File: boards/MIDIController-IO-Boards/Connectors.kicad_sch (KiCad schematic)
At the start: 26 parts, among them J1 KeyboardCtrl, J2 TechnicsCtrl, J3 StopLeftCtrl, J4 StopRightCtrl, J6 PanelCtrl, J7 ToeStudCtrl, U2 H11L1, U3 H11L1, U4 MAX3232

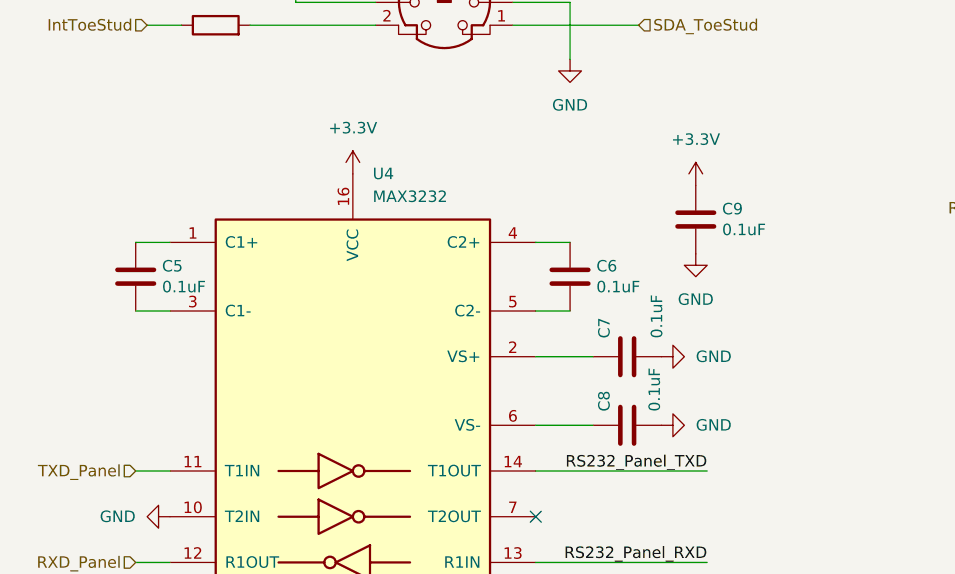
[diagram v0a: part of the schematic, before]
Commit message: Added bypass caps to power supplies, use cheaper MAX232 IC.
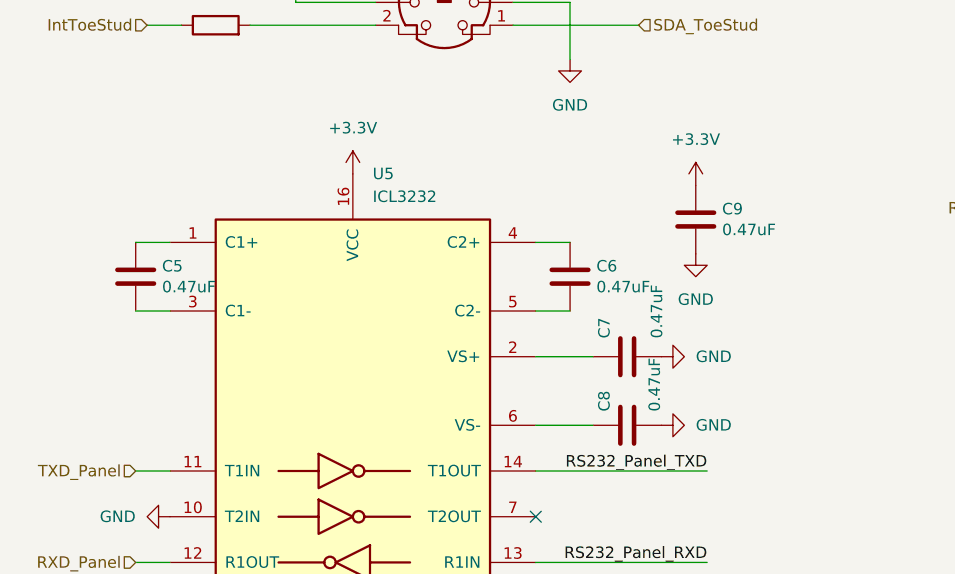
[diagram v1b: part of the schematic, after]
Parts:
- removed U4: MAX3232, Package_DIP:DIP-16_W7.62mm_Socket, symbol Interface_UART:MAX3232
- added U5: ICL3232, Package_DIP:DIP-16_W7.62mm, symbol Interface_UART:ICL3232
- C5, C6, C7, C8, C9: value 0.1uF -> 0.47uF
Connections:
- net +3.3V: now also U5.16 (VCC)
- net GND: now also U5.10 (T2IN), U5.15 (GND), U5.8 (R2IN)
- net RS232_Panel_RXD: now also U5.13 (R1IN)
- net RS232_Panel_TXD: now also U5.14 (T1OUT)
- net RXD_Panel: now also U5.12 (R1OUT)
- net TXD_Panel: now also U5.11 (T1IN)
- net at C6.1: now also U5.4 (C2+)
- net at C6.2: now also U5.5 (C2-)
- net at C5.1: now also U5.1 (C1+)
- net at C5.2: now also U5.3 (C1-)
- net at C7.1: now also U5.2 (VS+)
- net at C8.1: now also U5.6 (VS-)
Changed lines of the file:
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@@
+	)
+	(symbol
+		(lib_id "Interface_UART:ICL3232")
+		(at 142.24 125.73 0)
+		(unit 1)
+		(exclude_from_sim no)
+		(in_bom yes)
+		(on_board yes)
+		(dnp no)
+		(fields_autoplaced yes)
+		(property "Reference" "U5"
+			(at 144.4341 95.25 0)
+			(effects
+				(font
+					(size 1.27 1.27)
+				)
+				(justify left)
+			)
+		)
+		(property "Value" "ICL3232"
+			(at 144.4341 97.79 0)
+			(effects
+				(font
+					(size 1.27 1.27)
+				)
+				(justify left)
+			)
+		)
+		(property "Footprint" "Package_DIP:DIP-16_W7.62mm"
+			(at 143.51 152.4 0)
+			(effects
+				(font
+					(size 1.27 1.27)
+				)
+				(justify left)
+				(hide yes)
+			)
+		)
+		(property "Datasheet" "http://www.intersil.com/content/dam/Intersil/documents/icl3/icl3221-22-23-32-41-43.pdf"
+			(at 142.24 123.19 0)
+			(effects
+				(font
+					(size 1.27 1.27)
+				)
+				(hide yes)
+			)
+		)
+		(property "Description" "3.0V to 5.5V, Low-Power, up to 250kbps, True RS-232 Transceivers Using Four 0.1μF External Capacitors"
+			(at 142.24 125.73 0)
+			(effects
+				(font
+					(size 1.27 1.27)
+				)
+				(hide yes)
+			)
+		)
+		(pin "3"
+		)
+		(pin "8"
+		)
+		(pin "4"
+		)
+		(pin "2"
+		)
+		(pin "6"
+		)
+		(pin "7"
+		)
+		(pin "9"
+		)
+		(pin "5"
+		)
+		(pin "16"
+		)
+		(pin "14"
+		)
+		(pin "1"
+		)
+		(pin "15"
+		)
+		(pin "11"
+		)
+		(pin "12"
+		)
+		(pin "10"
+		)
+		(pin "13"
+		)
+		(instances
+			(project "MIDIController-IO-Boards"
+				(path "/06df47e9-b50a-4827-8ccb-76595e56d621/563c44a9-e62f-4884-9575-68843445bbb7"
+					(reference "U5")
+					(unit 1)
+				)
+			)
+		)
 	)
 	(symbol
@@
 			)
 		)
-		(property "Value" "0.1uF"
+		(property "Value" "0.47uF"
 			(at 183.261 101.473 0)
 			(effects
@@
 			)
 		)
-		(property "Value" "0.1uF"
+		(property "Value" "0.47uF"
 			(at 169.291 107.823 0)
 			(effects
@@
 			)
 		)
-		(property "Value" "0.1uF"
+		(property "Value" "0.47uF"
 			(at 121.031 107.823 0)
 			(effects
@@
 	)
 	(symbol
-		(lib_id "Interface_UART:MAX3232")
-		(at 142.24 125.73 0)
-		(unit 1)
-		(exclude_from_sim no)
-		(in_bom yes)
-		(on_board yes)
-		(dnp no)
-		(fields_autoplaced yes)
-		(property "Reference" "U4"
-			(at 144.4341 95.25 0)
-			(effects
-				(font
-					(size 1.27 1.27)
-				)
-				(justify left)
-			)
-		)
-		(property "Value" "MAX3232"
-			(at 144.4341 97.79 0)
-			(effects
-				(font
-					(size 1.27 1.27)
-				)
-				(justify left)
-			)
-		)
-		(property "Footprint" "Package_DIP:DIP-16_W7.62mm_Socket"
-			(at 143.51 152.4 0)
-			(effects
-				(font
-					(size 1.27 1.27)
-				)
-				(justify left)
-				(hide yes)
-			)
-		)
-		(property "Datasheet" "https://datasheets.maximintegrated.com/en/ds/MAX3222-MAX3241.pdf"
-			(at 142.24 123.19 0)
-			(effects
-				(font
-					(size 1.27 1.27)
-				)
-				(hide yes)
-			)
-		)
-		(property "Description" "3.0V to 5.5V, Low-Power, up to 1Mbps, True RS-232 Transceivers Using Four 0.1μF External Capacitors"
-			(at 142.24 125.73 0)
-			(effects
-				(font
-					(size 1.27 1.27)
-				)
-				(hide yes)
-			)
-		)
-		(pin "2"
-		)
-		(pin "9"
-		)
-		(pin "4"
-		)
-		(pin "7"
-		)
-		(pin "5"
-		)
-		(pin "10"
-		)
-		(pin "11"
-		)
-		(pin "1"
-		)
-		(pin "8"
-		)
-		(pin "6"
-		)
-		(pin "3"
-		)
-		(pin "16"
-		)
-		(pin "13"
-		)
-		(pin "14"
-		)
-		(pin "12"
-		)
-		(pin "15"
-		)
-		(instances
-			(project "MIDIController-IO-Boards"
-				(path "/06df47e9-b50a-4827-8ccb-76595e56d621/563c44a9-e62f-4884-9575-68843445bbb7"
-					(reference "U4")
-					(unit 1)
-				)
-			)
-		)
-	)
-	(symbol
 		(lib_id "Device:R")
 		(at 54.61 46.99 90)
@@
 			)
 		)
-		(property "Value" "0.1uF"
+		(property "Value" "0.47uF"
 			(at 175.768 121.666 0)
 			(effects
@@
 			)
 		)
-		(property "Value" "0.1uF"
+		(property "Value" "0.47uF"
 			(at 176.022 113.538 0)
 			(effects

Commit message: Updated design rules to 0.32mm template and exported Gerber files
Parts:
- C5, C6, C7, C8, C9: footprint Capacitor_THT:C_Rect_L4.6mm_W3.0mm_P2.50mm_MKS02_FKP02 -> Capacitor_THT:C_Rect_L7.0mm_W3.5mm_P5.00mm
- R1, R10, R2, R3, R7, R8, R9: footprint Resistor_THT:R_Axial_DIN0204_L3.6mm_D1.6mm_P7.62mm_Horizontal -> Resistor_THT:R_Axial_DIN0207_L6.3mm_D2.5mm_P10.16mm_Horizontal
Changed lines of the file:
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@@
 			)
 		)
-		(property "Footprint" "Capacitor_THT:C_Rect_L4.6mm_W3.0mm_P2.50mm_MKS02_FKP02"
+		(property "Footprint" "Capacitor_THT:C_Rect_L7.0mm_W3.5mm_P5.00mm"
 			(at 181.3052 104.14 0)
 			(effects
@@
 			)
 		)
-		(property "Footprint" "Resistor_THT:R_Axial_DIN0204_L3.6mm_D1.6mm_P7.62mm_Horizontal"
+		(property "Footprint" "Resistor_THT:R_Axial_DIN0207_L6.3mm_D2.5mm_P10.16mm_Horizontal"
 			(at 228.092 93.98 90)
 			(effects
@@
 			)
 		)
-		(property "Footprint" "Capacitor_THT:C_Rect_L4.6mm_W3.0mm_P2.50mm_MKS02_FKP02"
+		(property "Footprint" "Capacitor_THT:C_Rect_L7.0mm_W3.5mm_P5.00mm"
 			(at 167.3352 110.49 0)
 			(effects
@@
 			)
 		)
-		(property "Footprint" "Resistor_THT:R_Axial_DIN0204_L3.6mm_D1.6mm_P7.62mm_Horizontal"
+		(property "Footprint" "Resistor_THT:R_Axial_DIN0207_L6.3mm_D2.5mm_P10.16mm_Horizontal"
 			(at 54.61 113.538 90)
 			(effects
@@
 			)
 		)
-		(property "Footprint" "Capacitor_THT:C_Rect_L4.6mm_W3.0mm_P2.50mm_MKS02_FKP02"
+		(property "Footprint" "Capacitor_THT:C_Rect_L7.0mm_W3.5mm_P5.00mm"
 			(at 119.0752 110.49 0)
 			(effects
@@
 			)
 		)
-		(property "Footprint" "Resistor_THT:R_Axial_DIN0204_L3.6mm_D1.6mm_P7.62mm_Horizontal"
+		(property "Footprint" "Resistor_THT:R_Axial_DIN0207_L6.3mm_D2.5mm_P10.16mm_Horizontal"
 			(at 54.61 80.518 90)
 			(effects
@@
 			)
 		)
-		(property "Footprint" "Resistor_THT:R_Axial_DIN0204_L3.6mm_D1.6mm_P7.62mm_Horizontal"
+		(property "Footprint" "Resistor_THT:R_Axial_DIN0207_L6.3mm_D2.5mm_P10.16mm_Horizontal"
 			(at 254.762 38.1 90)
 			(effects
@@
 			)
 		)
-		(property "Footprint" "Resistor_THT:R_Axial_DIN0204_L3.6mm_D1.6mm_P7.62mm_Horizontal"
+		(property "Footprint" "Resistor_THT:R_Axial_DIN0207_L6.3mm_D2.5mm_P10.16mm_Horizontal"
 			(at 252.222 91.44 90)
 			(effects
@@
 			)
 		)
-		(property "Footprint" "Resistor_THT:R_Axial_DIN0204_L3.6mm_D1.6mm_P7.62mm_Horizontal"
+		(property "Footprint" "Resistor_THT:R_Axial_DIN0207_L6.3mm_D2.5mm_P10.16mm_Horizontal"
 			(at 54.61 48.768 90)
 			(effects
@@
 			)
 		)
-		(property "Footprint" "Resistor_THT:R_Axial_DIN0204_L3.6mm_D1.6mm_P7.62mm_Horizontal"
+		(property "Footprint" "Resistor_THT:R_Axial_DIN0207_L6.3mm_D2.5mm_P10.16mm_Horizontal"
 			(at 230.632 40.64 90)
 			(effects
@@
 			)
 		)
-		(property "Footprint" "Capacitor_THT:C_Rect_L4.6mm_W3.0mm_P2.50mm_MKS02_FKP02"
+		(property "Footprint" "Capacitor_THT:C_Rect_L7.0mm_W3.5mm_P5.00mm"
 			(at 176.53 122.2248 0)
 			(effects
@@
 			)
 		)
-		(property "Footprint" "Capacitor_THT:C_Rect_L4.6mm_W3.0mm_P2.50mm_MKS02_FKP02"
+		(property "Footprint" "Capacitor_THT:C_Rect_L7.0mm_W3.5mm_P5.00mm"
 			(at 176.53 114.6048 0)
 			(effects

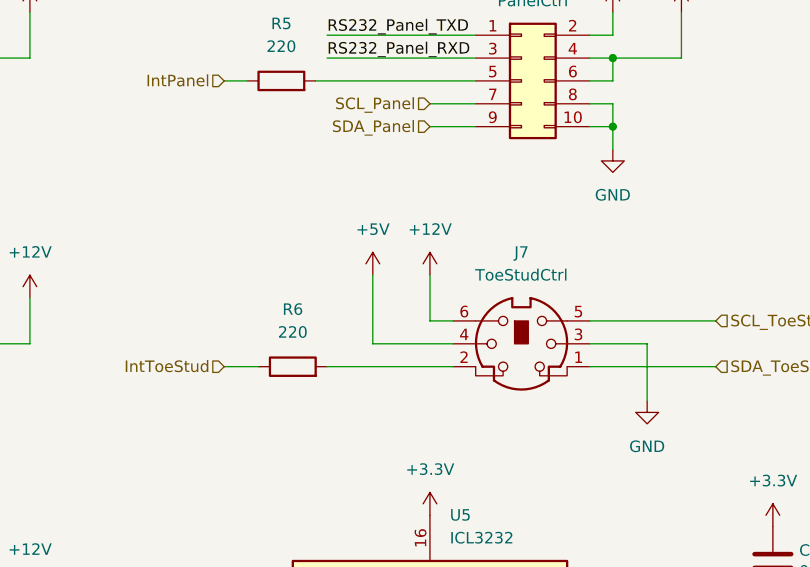
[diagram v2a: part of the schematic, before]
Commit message: Make Toestud PS2 connectors symmetrical to avoid connection errors
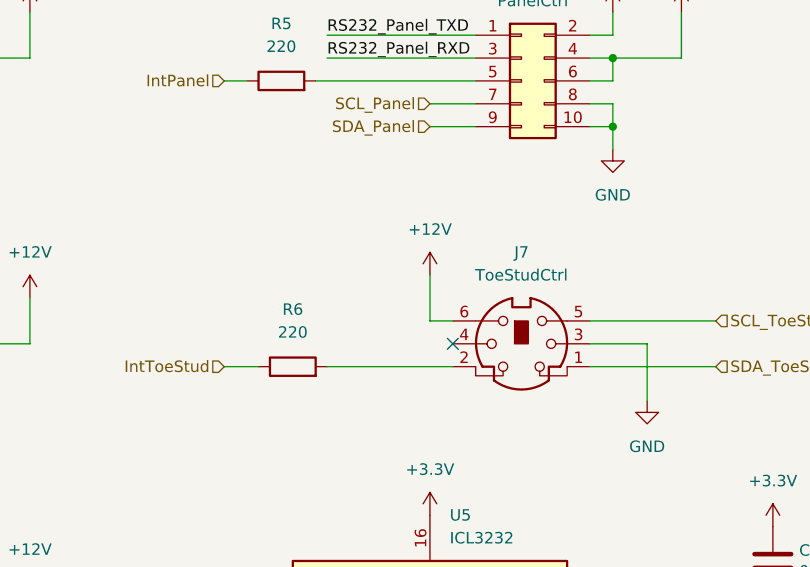
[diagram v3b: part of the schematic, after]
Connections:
- net +5V: no longer J7.4
- no-connect marks 8 -> 9
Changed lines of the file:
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@@
+	)
+	(no_connect
+		(at 144.78 76.2)
 	)
 	(no_connect
@@
 	(wire
 		(pts
-			(xy 144.78 76.2) (xy 135.89 76.2)
-		)
-		(stroke
-			(width 0)
-			(type default)
-		)
-	)
-	(wire
-		(pts
 			(xy 58.42 76.2) (xy 74.93 76.2)
 		)
@@
 		(pts
 			(xy 256.54 41.91) (xy 256.54 43.18)
-		)
-		(stroke
-			(width 0)
-			(type default)
-		)
-	)
-	(wire
-		(pts
-			(xy 135.89 76.2) (xy 135.89 68.58)
 		)
 		(stroke
@@
 					(unit 1)
 				)
-			)
-		)
-	)
-	(symbol
-		(lib_id "power:+5V")
-		(at 135.89 68.58 0)
-		(unit 1)
-		(exclude_from_sim no)
-		(in_bom yes)
-		(on_board yes)
-		(dnp no)
-		(fields_autoplaced yes)
-		(property "Reference" "#PWR016"
-			(at 135.89 72.39 0)
-			(effects
-				(font
-					(size 1.27 1.27)
-				)
-				(hide yes)
-			)
-		)
-		(property "Value" "+5V"
-			(at 135.89 63.5 0)
-			(effects
-				(font
-					(size 1.27 1.27)
-				)
-			)
-		)
-		(property "Footprint" ""
-			(at 135.89 68.58 0)
-			(effects
-				(font
-					(size 1.27 1.27)
-				)
-				(hide yes)
-			)
-		)
-		(property "Datasheet" ""
-			(at 135.89 68.58 0)
-			(effects
-				(font
-					(size 1.27 1.27)
-				)
-				(hide yes)
-			)
-		)
-		(property "Description" "Power symbol creates a global label with name \"+5V\""
-			(at 135.89 68.58 0)
-			(effects
-				(font
-					(size 1.27 1.27)
-				)
-				(hide yes)
-			)
-		)
-		(pin "1"
-		)
-		(instances
-			(project "MIDIController-IO-Boards"
-				(path "/06df47e9-b50a-4827-8ccb-76595e56d621/563c44a9-e62f-4884-9575-68843445bbb7"
-					(reference "#PWR016")
-					(unit 1)
-				)
